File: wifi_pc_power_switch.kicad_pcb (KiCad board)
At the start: 2 copper layers, 51.8 x 52.8 mm, 20 parts, among them J1 Conn_01x04_Socket, J2 Conn_01x04_Socket, J3 Conn_01x04_Socket, J4 Conn_01x04_Socket, Q1 BSS123, SW1 SW_Push, U1 TLP175A

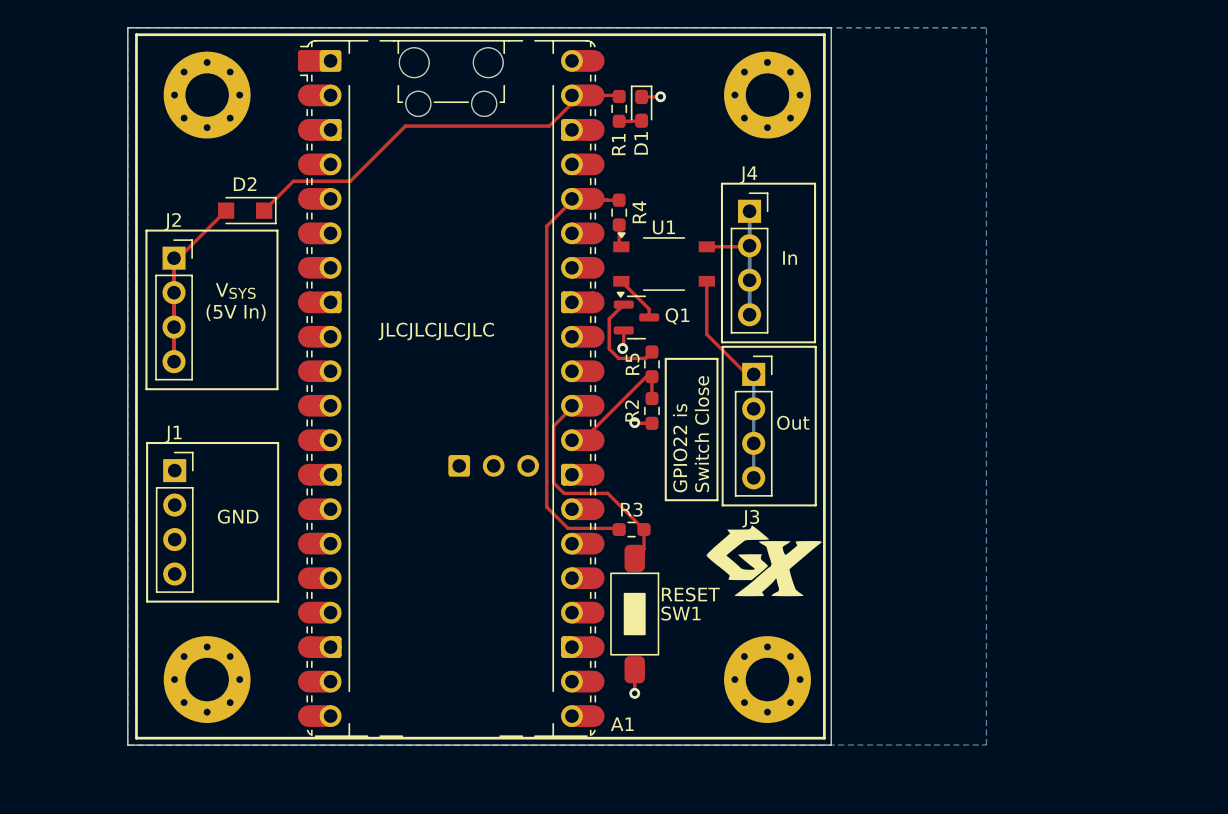
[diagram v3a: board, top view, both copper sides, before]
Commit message: We don't need that many pins, add sense
 - Reduce the 4x pins to 2x, and place them near the edge (to be used
   with simple screw terminals)
 - Add a sense line, so the MCU can tell if the computer is on. It needs
   a pulldown due to rp2350 E9 errata.
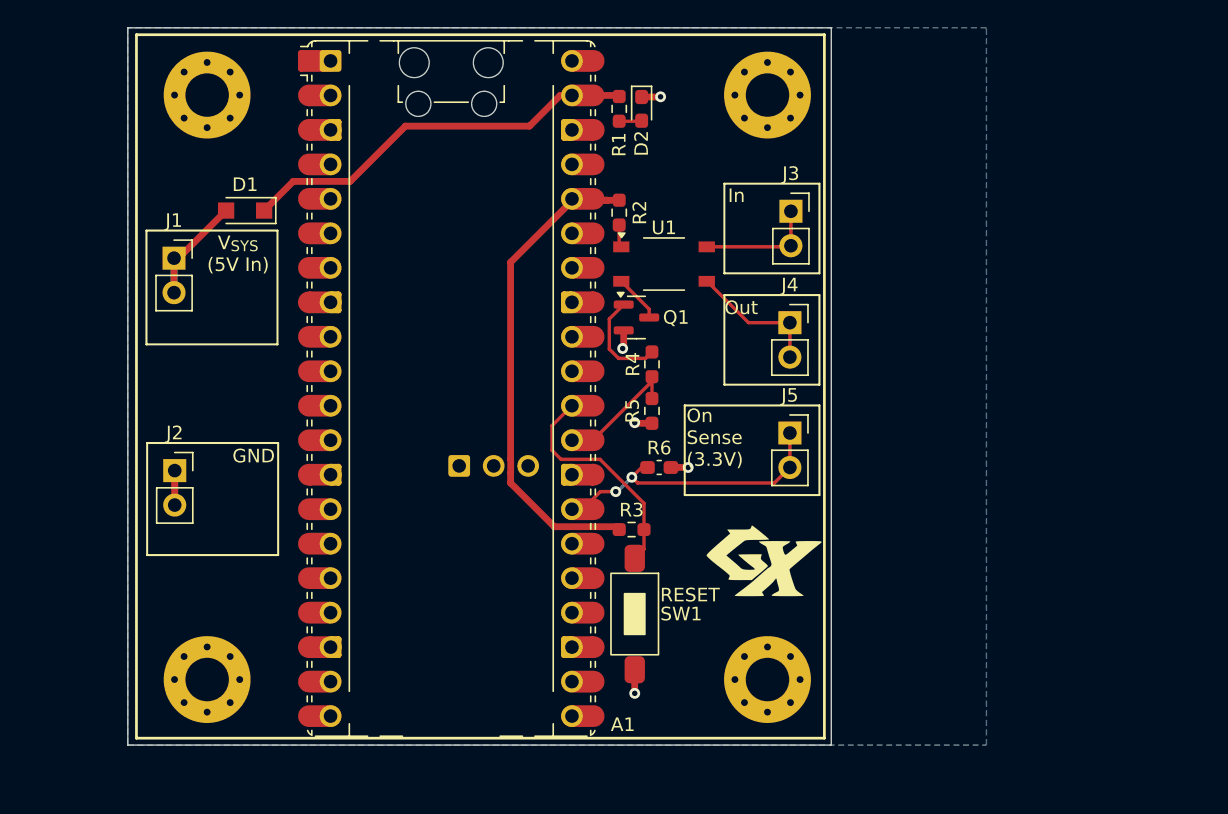
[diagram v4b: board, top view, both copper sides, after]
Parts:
- added J5: ON, Connector_PinSocket_2.54mm:PinSocket_1x02_P2.54mm_Vertical, F.Cu at (188.2, 105.0)
- added R6: 5.11k, Capacitor_SMD:C_0603_1608Metric_Pad1.08x0.95mm_HandSolder, F.Cu at (178.6, 107.6)
- A1: value RaspberryPi_Pico_W -> RaspberryPi_Pico_2_W
- J1: renamed from J2; value Conn_01x04_Socket -> V_{in}; footprint Connector_PinSocket_2.54mm:PinSocket_1x04_P2.54mm_Vertical -> Connector_PinSocket_2.54mm:PinSocket_1x02_P2.54mm_Vertical
- J2: renamed from J1; value Conn_01x04_Socket -> GND; footprint Connector_PinSocket_2.54mm:PinSocket_1x04_P2.54mm_Vertical -> Connector_PinSocket_2.54mm:PinSocket_1x02_P2.54mm_Vertical
- J3: renamed from J4; value Conn_01x04_Socket -> IN; footprint Connector_PinSocket_2.54mm:PinSocket_1x04_P2.54mm_Vertical -> Connector_PinSocket_2.54mm:PinSocket_1x02_P2.54mm_Vertical
- J4: renamed from J3; value Conn_01x04_Socket -> OUT; footprint Connector_PinSocket_2.54mm:PinSocket_1x04_P2.54mm_Vertical -> Connector_PinSocket_2.54mm:PinSocket_1x02_P2.54mm_Vertical
- moved J4 4.65 mm to (188.2, 96.9)
- moved J3 3.05 mm to (188.3, 88.7)
- renumbered D2 to D1, D1 to D2, H3 to H2, H2 to H3, R4 to R2, R5 to R4, R2 to R5
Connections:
- A1 pad 27: unconnected-(A1-GPIO21-Pad27) -> /ON
- D1 pad 2: Net-(D2-A) (its old number) -> /V_{in}
- J1 pad 1: Net-(D2-A) (its old number) -> /V_{in}
- J1 pad 2: Net-(D2-A) (its old number) -> /V_{in}
- J3 pad 1: Net-(J4-Pin_1) -> Net-(J3-Pin_1)
- J3 pad 2: Net-(J4-Pin_1) -> Net-(J3-Pin_1)
- J4 pad 1: Net-(J3-Pin_1) -> Net-(J4-Pin_1)
- J4 pad 2: Net-(J3-Pin_1) -> Net-(J4-Pin_1)
- U1 pad 4: Net-(J3-Pin_1) -> Net-(J4-Pin_1)
- U1 pad 6: Net-(J4-Pin_1) -> Net-(J3-Pin_1)
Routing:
- net /ON: track 0.00 -> 23.4 mm, vias 0 -> 2
- net Net-(D2-A) (its old number): track 20.5 -> 0.00 mm
- net /V_{in}: track 0.00 -> 10.0 mm
- net GND: track 5.80 -> 12.2 mm, vias 4 -> 5
- net Net-(J4-Pin_1): track 18.4 -> 12.4 mm
- net Net-(J3-Pin_1): track 16.2 -> 11.2 mm
- net /V_{3.3}: track 35.5 -> 37.8 mm
- net /EN: track 8.63 -> 7.75 mm
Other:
- board text added: "On Sense (3.3V)"
- board text removed: "GPIO22 is Switch Close"
- board text removed: "JLCJLCJLCJLC"
